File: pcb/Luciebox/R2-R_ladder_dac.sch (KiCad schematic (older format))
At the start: 12 parts, among them T2 terminal_8x1, T3 terminal_8x1, T4 terminal_8x1

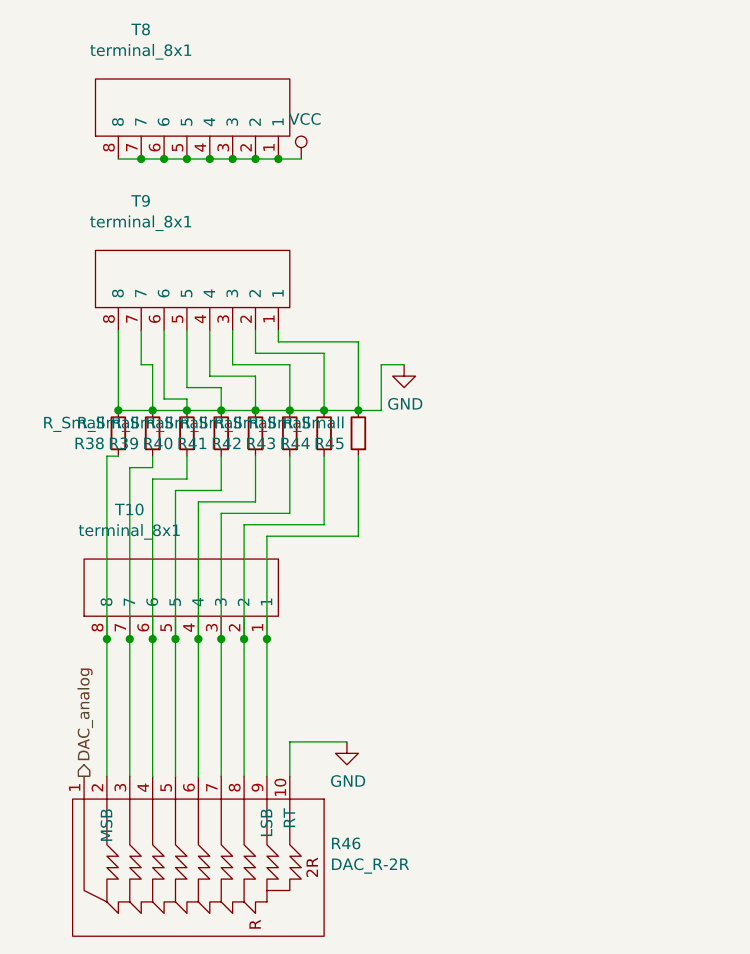
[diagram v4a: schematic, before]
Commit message: buttons and selector switch debugging. Starting to change pcb schematic for v2.0 board
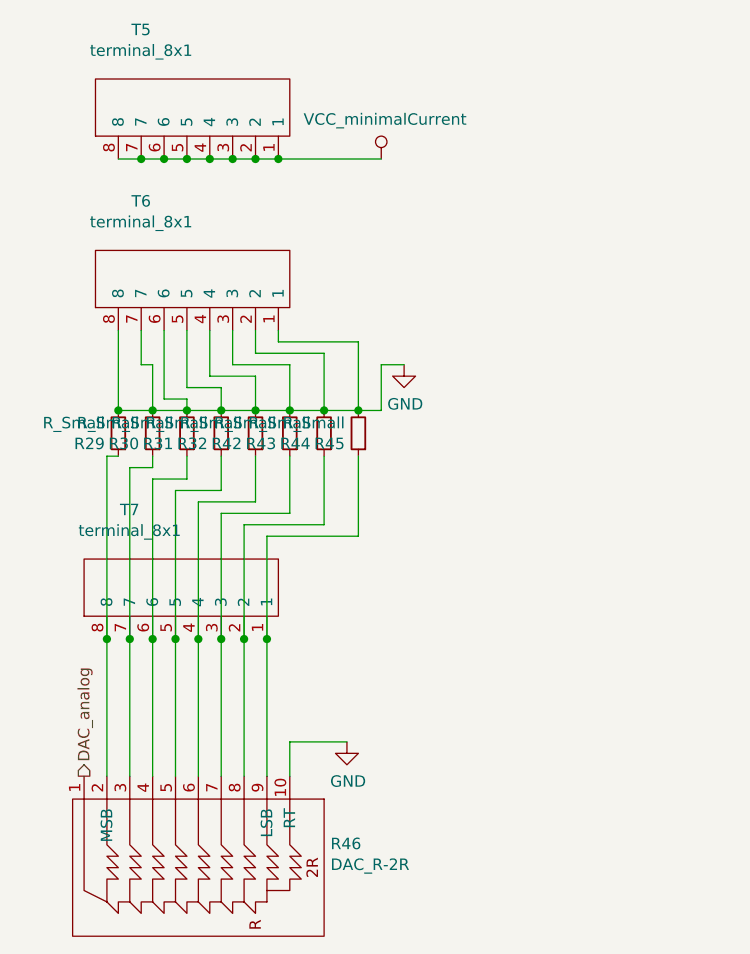
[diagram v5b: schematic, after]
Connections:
- net VCC renamed VCC_minimalCurrent
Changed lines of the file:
@@
 EESchema Schematic File Version 4
 LIBS:Luciebox-cache
-EELAYER 29 0
+EELAYER 30 0
 EELAYER END
 $Descr A4 11693 8268
@@
 AR Path="/5D761BCA/5D7526ED" Ref="R32"  Part="1"
 AR Path="/5D9307E8/5D7526ED" Ref="R41"  Part="1"
-F 0 "R41" H 3109 2246 50  0000 L CNN
+F 0 "R32" H 3109 2246 50  0000 L CNN
 F 1 "R_Small" H 3109 2155 50  0000 L CNN
 F 2 "Luciebox:1206" H 3050 2200 50  0001 C CNN
@@
 AR Path="/5D761BCA/5D7526F3" Ref="R31"  Part="1"
 AR Path="/5D9307E8/5D7526F3" Ref="R40"  Part="1"
-F 0 "R40" H 2959 2246 50  0000 L CNN
+F 0 "R31" H 2959 2246 50  0000 L CNN
 F 1 "R_Small" H 2959 2155 50  0000 L CNN
 F 2 "Luciebox:1206" H 2900 2200 50  0001 C CNN
@@
 AR Path="/5D761BCA/5D7526F9" Ref="R30"  Part="1"
 AR Path="/5D9307E8/5D7526F9" Ref="R39"  Part="1"
-F 0 "R39" H 2809 2246 50  0000 L CNN
+F 0 "R30" H 2809 2246 50  0000 L CNN
 F 1 "R_Small" H 2809 2155 50  0000 L CNN
 F 2 "Luciebox:1206" H 2750 2200 50  0001 C CNN
@@
 AR Path="/5D761BCA/5D75277B" Ref="#PWR023"  Part="1"
 AR Path="/5D9307E8/5D75277B" Ref="#PWR026"  Part="1"
-F 0 "#PWR026" H 3850 1650 50  0001 C CNN
+F 0 "#PWR023" H 3850 1650 50  0001 C CNN
 F 1 "GND" H 3855 1727 50  0000 C CNN
 F 2 "" H 3850 1900 50  0001 C CNN
@@
 AR Path="/5D761BCA/5D7527B8" Ref="R29"  Part="1"
 AR Path="/5D9307E8/5D7527B8" Ref="R38"  Part="1"
-F 0 "R38" H 2659 2246 50  0000 L CNN
+F 0 "R29" H 2659 2246 50  0000 L CNN
 F 1 "R_Small" H 2659 2155 50  0000 L CNN
 F 2 "Luciebox:1206" H 2600 2200 50  0001 C CNN
@@
 AR Path="/5D761BCA/5D7526D5" Ref="T7"  Part="1"
 AR Path="/5D9307E8/5D7526D5" Ref="T10"  Part="1"
-F 0 "T10" V 3765 3650 50  0000 C CNN
+F 0 "T7" V 3765 3650 50  0000 C CNN
 F 1 "terminal_8x1" V 3674 3650 50  0000 C CNN
 F 2 "Luciebox:Terminal_8x1_100mil" H 3250 3050 50  0001 C CNN
@@
 AR Path="/5D761BCA/5DACA23D" Ref="#PWR024"  Part="1"
 AR Path="/5D9307E8/5DACA23D" Ref="#PWR027"  Part="1"
-F 0 "#PWR027" H 3600 3300 50  0001 C CNN
+F 0 "#PWR024" H 3600 3300 50  0001 C CNN
 F 1 "GND" H 3605 3377 50  0000 C CNN
 F 2 "" H 3600 3550 50  0001 C CNN
@@
 AR Path="/5D761BCA/5DAEA72B" Ref="T6"  Part="1"
 AR Path="/5D9307E8/5DAEA72B" Ref="T9"  Part="1"
-F 0 "T9" V 3815 2300 50  0000 C CNN
+F 0 "T6" V 3815 2300 50  0000 C CNN
 F 1 "terminal_8x1" V 3724 2300 50  0000 C CNN
 F 2 "Luciebox:Terminal_8x1_100mil" H 3300 1700 50  0001 C CNN
@@
 AR Path="/5D761BCA/5DB0039D" Ref="T5"  Part="1"
 AR Path="/5D9307E8/5DB0039D" Ref="T8"  Part="1"
-F 0 "T8" V 3815 1550 50  0000 C CNN
+F 0 "T5" V 3815 1550 50  0000 C CNN
 F 1 "terminal_8x1" V 3724 1550 50  0000 C CNN
 F 2 "Luciebox:Terminal_8x1_100mil" H 3300 950 50  0001 C CNN
@@
 Wire Wire Line
 	3200 1000 3100 1000
-Wire Wire Line
-	3300 1000 3400 1000
 Connection ~ 3300 1000
 $Comp
-L power:VCC #PWR025
+L Luciebox_components:VCC_minimalCurrent #PWR025
 U 1 1 5DB05874
-P 3400 1000
+P 3750 1000
 AR Path="/5D9307E8/5DB05874" Ref="#PWR025"  Part="1"
 AR Path="/5D74964C/5DB05874" Ref="#PWR019"  Part="1"
 AR Path="/5D761BCA/5DB05874" Ref="#PWR022"  Part="1"
-F 0 "#PWR025" H 3400 850 50  0001 C CNN
-F 1 "VCC" H 3417 1173 50  0000 C CNN
-F 2 "" H 3400 1000 50  0001 C CNN
-F 3 "" H 3400 1000 50  0001 C CNN
-	1    3400 1000
+F 0 "#PWR022" H 3750 850 50  0001 C CNN
+F 1 "VCC_minimalCurrent" H 3767 1173 50  0000 C CNN
+F 2 "" H 3750 1000 50  0001 C CNN
+F 3 "" H 3750 1000 50  0001 C CNN
+	1    3750 1000
 	1    0    0    -1
 $EndComp
+Wire Wire Line
+	3300 1000 3750 1000
 $EndSCHEMATC

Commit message: changes in pcb v2.0
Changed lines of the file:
@@
 EESchema Schematic File Version 4
 LIBS:Luciebox-cache
-EELAYER 30 0
+EELAYER 29 0
 EELAYER END
 $Descr A4 11693 8268
 encoding utf-8
-Sheet 3 4
+Sheet 2 4
 Title ""
 Date ""
@@
 AR Path="/5D761BCA/5D7526CF" Ref="R36"  Part="1"
 AR Path="/5D9307E8/5D7526CF" Ref="R45"  Part="1"
-F 0 "R45" H 3709 2246 50  0000 L CNN
+F 0 "R36" H 3709 2246 50  0000 L CNN
 F 1 "R_Small" H 3709 2155 50  0000 L CNN
 F 2 "Luciebox:1206" H 3650 2200 50  0001 C CNN
@@
 $Comp
 L Device:R_Small R26
-U 1 1 5D7526DB
+U 1 1 5E6454DF
 P 3500 2200
-AR Path="/5D74964C/5D7526DB" Ref="R26"  Part="1"
-AR Path="/5D761BCA/5D7526DB" Ref="R35"  Part="1"
-AR Path="/5D9307E8/5D7526DB" Ref="R44"  Part="1"
-F 0 "R44" H 3559 2246 50  0000 L CNN
+AR Path="/5D74964C/5E6454DF" Ref="R26"  Part="1"
+AR Path="/5D761BCA/5E6454DF" Ref="R35"  Part="1"
+AR Path="/5D9307E8/5E6454DF" Ref="R44"  Part="1"
+F 0 "R35" H 3559 2246 50  0000 L CNN
 F 1 "R_Small" H 3559 2155 50  0000 L CNN
 F 2 "Luciebox:1206" H 3500 2200 50  0001 C CNN
@@
 $Comp
 L Device:R_Small R25
-U 1 1 5D7526E1
+U 1 1 5E6454E0
 P 3350 2200
-AR Path="/5D74964C/5D7526E1" Ref="R25"  Part="1"
-AR Path="/5D761BCA/5D7526E1" Ref="R34"  Part="1"
-AR Path="/5D9307E8/5D7526E1" Ref="R43"  Part="1"
-F 0 "R43" H 3409 2246 50  0000 L CNN
+AR Path="/5D74964C/5E6454E0" Ref="R25"  Part="1"
+AR Path="/5D761BCA/5E6454E0" Ref="R34"  Part="1"
+AR Path="/5D9307E8/5E6454E0" Ref="R43"  Part="1"
+F 0 "R34" H 3409 2246 50  0000 L CNN
 F 1 "R_Small" H 3409 2155 50  0000 L CNN
 F 2 "Luciebox:1206" H 3350 2200 50  0001 C CNN
@@
 $Comp
 L Device:R_Small R24
-U 1 1 5D7526E7
+U 1 1 5E6454E1
 P 3200 2200
-AR Path="/5D74964C/5D7526E7" Ref="R24"  Part="1"
-AR Path="/5D761BCA/5D7526E7" Ref="R33"  Part="1"
-AR Path="/5D9307E8/5D7526E7" Ref="R42"  Part="1"
-F 0 "R42" H 3259 2246 50  0000 L CNN
+AR Path="/5D74964C/5E6454E1" Ref="R24"  Part="1"
+AR Path="/5D761BCA/5E6454E1" Ref="R33"  Part="1"
+AR Path="/5D9307E8/5E6454E1" Ref="R42"  Part="1"
+F 0 "R33" H 3259 2246 50  0000 L CNN
 F 1 "R_Small" H 3259 2155 50  0000 L CNN
 F 2 "Luciebox:1206" H 3200 2200 50  0001 C CNN
@@
 $Comp
 L Luciebox_components:DAC_R-2R R28
-U 1 1 5DABC300
+U 1 1 5E6454E2
 P 2450 3700
-AR Path="/5D74964C/5DABC300" Ref="R28"  Part="1"
-AR Path="/5D761BCA/5DABC300" Ref="R37"  Part="1"
-AR Path="/5D9307E8/5DABC300" Ref="R46"  Part="1"
-F 0 "R46" V 2746 4778 50  0000 L CNN
+AR Path="/5D74964C/5E6454E2" Ref="R28"  Part="1"
+AR Path="/5D761BCA/5E6454E2" Ref="R37"  Part="1"
+AR Path="/5D9307E8/5E6454E2" Ref="R46"  Part="1"
+F 0 "R37" V 2746 4778 50  0000 L CNN
 F 1 "DAC_R-2R" V 2837 4778 50  0000 L CNN
 F 2 "Luciebox:SIP-10" H 2450 3700 50  0001 C CNN

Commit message: progressive change towards v2.0
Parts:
- R20, R21, R22, R23, R24, R25, R26, R27: footprint Luciebox:1206 -> Luciebox:1206_0805
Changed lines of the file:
@@
 $Descr A4 11693 8268
 encoding utf-8
-Sheet 2 4
+Sheet 3 4
 Title ""
 Date ""
@@
 F 0 "R36" H 3709 2246 50  0000 L CNN
 F 1 "R_Small" H 3709 2155 50  0000 L CNN
-F 2 "Luciebox:1206" H 3650 2200 50  0001 C CNN
+F 2 "Luciebox:1206_0805" H 3650 2200 50  0001 C CNN
 F 3 "~" H 3650 2200 50  0001 C CNN
 	1    3650 2200
@@
 F 0 "R35" H 3559 2246 50  0000 L CNN
 F 1 "R_Small" H 3559 2155 50  0000 L CNN
-F 2 "Luciebox:1206" H 3500 2200 50  0001 C CNN
+F 2 "Luciebox:1206_0805" H 3500 2200 50  0001 C CNN
 F 3 "~" H 3500 2200 50  0001 C CNN
 	1    3500 2200
@@
 F 0 "R34" H 3409 2246 50  0000 L CNN
 F 1 "R_Small" H 3409 2155 50  0000 L CNN
-F 2 "Luciebox:1206" H 3350 2200 50  0001 C CNN
+F 2 "Luciebox:1206_0805" H 3350 2200 50  0001 C CNN
 F 3 "~" H 3350 2200 50  0001 C CNN
 	1    3350 2200
@@
 F 0 "R33" H 3259 2246 50  0000 L CNN
 F 1 "R_Small" H 3259 2155 50  0000 L CNN
-F 2 "Luciebox:1206" H 3200 2200 50  0001 C CNN
+F 2 "Luciebox:1206_0805" H 3200 2200 50  0001 C CNN
 F 3 "~" H 3200 2200 50  0001 C CNN
 	1    3200 2200
@@
 F 0 "R32" H 3109 2246 50  0000 L CNN
 F 1 "R_Small" H 3109 2155 50  0000 L CNN
-F 2 "Luciebox:1206" H 3050 2200 50  0001 C CNN
+F 2 "Luciebox:1206_0805" H 3050 2200 50  0001 C CNN
 F 3 "~" H 3050 2200 50  0001 C CNN
 	1    3050 2200
@@
 F 0 "R31" H 2959 2246 50  0000 L CNN
 F 1 "R_Small" H 2959 2155 50  0000 L CNN
-F 2 "Luciebox:1206" H 2900 2200 50  0001 C CNN
+F 2 "Luciebox:1206_0805" H 2900 2200 50  0001 C CNN
 F 3 "~" H 2900 2200 50  0001 C CNN
 	1    2900 2200
@@
 F 0 "R30" H 2809 2246 50  0000 L CNN
 F 1 "R_Small" H 2809 2155 50  0000 L CNN
-F 2 "Luciebox:1206" H 2750 2200 50  0001 C CNN
+F 2 "Luciebox:1206_0805" H 2750 2200 50  0001 C CNN
 F 3 "~" H 2750 2200 50  0001 C CNN
 	1    2750 2200
@@
 F 0 "R29" H 2659 2246 50  0000 L CNN
 F 1 "R_Small" H 2659 2155 50  0000 L CNN
-F 2 "Luciebox:1206" H 2600 2200 50  0001 C CNN
+F 2 "Luciebox:1206_0805" H 2600 2200 50  0001 C CNN
 F 3 "~" H 2600 2200 50  0001 C CNN
 	1    2600 2200

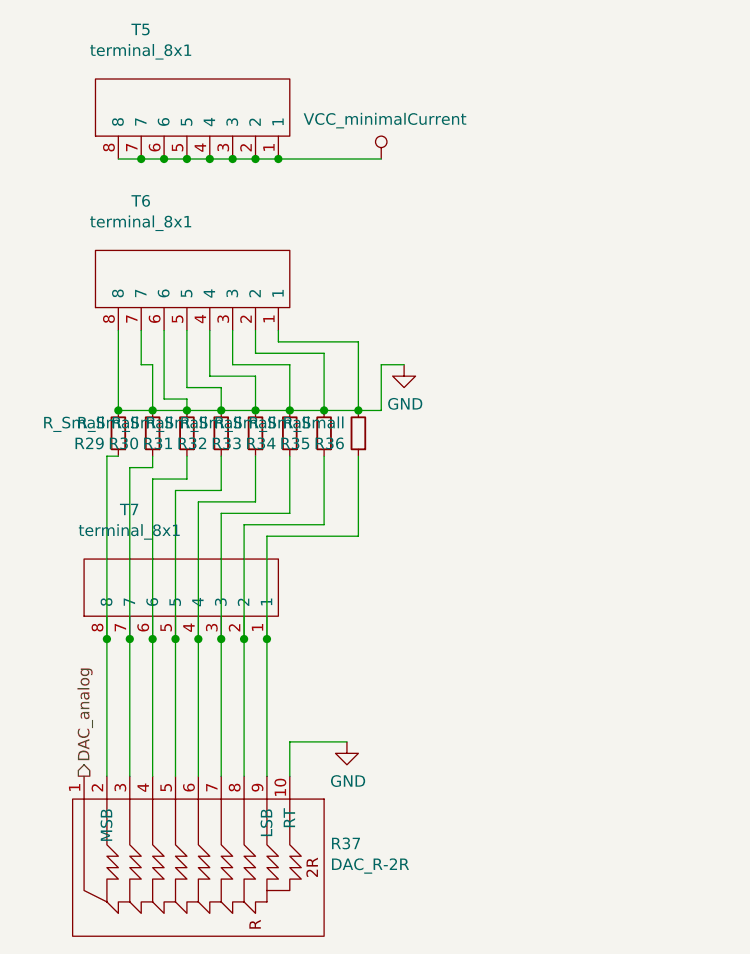
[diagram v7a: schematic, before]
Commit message: add holes for R-2R ladder, fix bug with tilt switch sheet. Set output led's. All good here.
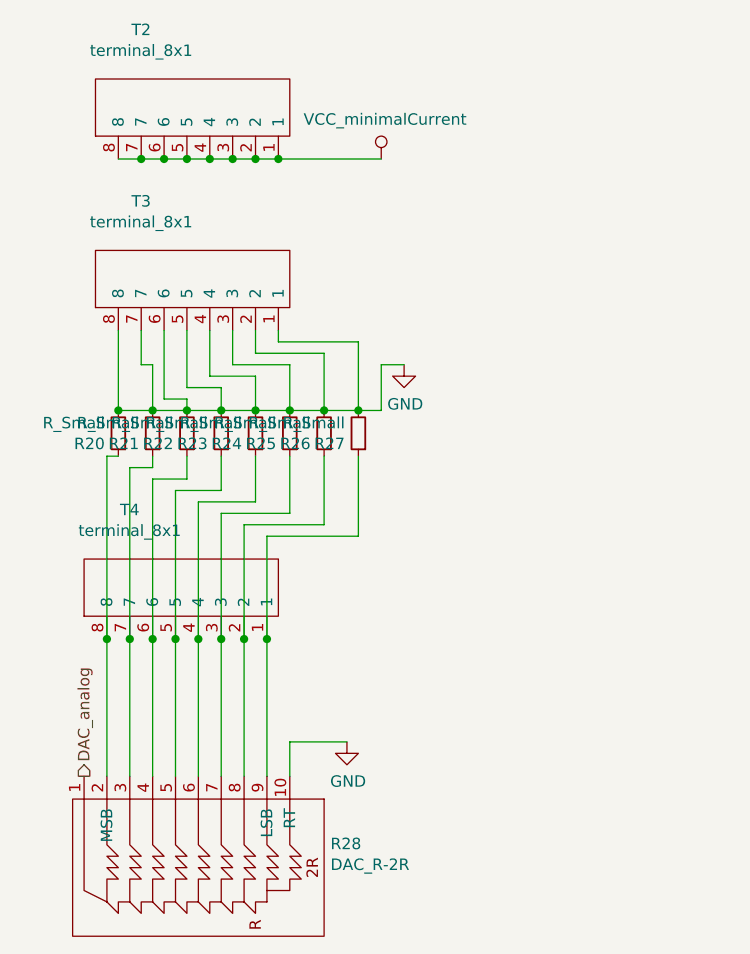
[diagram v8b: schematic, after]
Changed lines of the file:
@@
 $Descr A4 11693 8268
 encoding utf-8
-Sheet 3 4
+Sheet 2 4
 Title ""
 Date ""
@@
 AR Path="/5D761BCA/5D7526CF" Ref="R36"  Part="1"
 AR Path="/5D9307E8/5D7526CF" Ref="R45"  Part="1"
-F 0 "R36" H 3709 2246 50  0000 L CNN
+F 0 "R27" H 3709 2246 50  0000 L CNN
 F 1 "R_Small" H 3709 2155 50  0000 L CNN
 F 2 "Luciebox:1206_0805" H 3650 2200 50  0001 C CNN
@@
 AR Path="/5D761BCA/5E6454DF" Ref="R35"  Part="1"
 AR Path="/5D9307E8/5E6454DF" Ref="R44"  Part="1"
-F 0 "R35" H 3559 2246 50  0000 L CNN
+F 0 "R26" H 3559 2246 50  0000 L CNN
 F 1 "R_Small" H 3559 2155 50  0000 L CNN
 F 2 "Luciebox:1206_0805" H 3500 2200 50  0001 C CNN
@@
 AR Path="/5D761BCA/5E6454E0" Ref="R34"  Part="1"
 AR Path="/5D9307E8/5E6454E0" Ref="R43"  Part="1"
-F 0 "R34" H 3409 2246 50  0000 L CNN
+F 0 "R25" H 3409 2246 50  0000 L CNN
 F 1 "R_Small" H 3409 2155 50  0000 L CNN
 F 2 "Luciebox:1206_0805" H 3350 2200 50  0001 C CNN
@@
 AR Path="/5D761BCA/5E6454E1" Ref="R33"  Part="1"
 AR Path="/5D9307E8/5E6454E1" Ref="R42"  Part="1"
-F 0 "R33" H 3259 2246 50  0000 L CNN
+F 0 "R24" H 3259 2246 50  0000 L CNN
 F 1 "R_Small" H 3259 2155 50  0000 L CNN
 F 2 "Luciebox:1206_0805" H 3200 2200 50  0001 C CNN
@@
 AR Path="/5D761BCA/5D7526ED" Ref="R32"  Part="1"
 AR Path="/5D9307E8/5D7526ED" Ref="R41"  Part="1"
-F 0 "R32" H 3109 2246 50  0000 L CNN
+F 0 "R23" H 3109 2246 50  0000 L CNN
 F 1 "R_Small" H 3109 2155 50  0000 L CNN
 F 2 "Luciebox:1206_0805" H 3050 2200 50  0001 C CNN
@@
 AR Path="/5D761BCA/5D7526F3" Ref="R31"  Part="1"
 AR Path="/5D9307E8/5D7526F3" Ref="R40"  Part="1"
-F 0 "R31" H 2959 2246 50  0000 L CNN
+F 0 "R22" H 2959 2246 50  0000 L CNN
 F 1 "R_Small" H 2959 2155 50  0000 L CNN
 F 2 "Luciebox:1206_0805" H 2900 2200 50  0001 C CNN
@@
 AR Path="/5D761BCA/5D7526F9" Ref="R30"  Part="1"
 AR Path="/5D9307E8/5D7526F9" Ref="R39"  Part="1"
-F 0 "R30" H 2809 2246 50  0000 L CNN
+F 0 "R21" H 2809 2246 50  0000 L CNN
 F 1 "R_Small" H 2809 2155 50  0000 L CNN
 F 2 "Luciebox:1206_0805" H 2750 2200 50  0001 C CNN
@@
 AR Path="/5D761BCA/5D7527B8" Ref="R29"  Part="1"
 AR Path="/5D9307E8/5D7527B8" Ref="R38"  Part="1"
-F 0 "R29" H 2659 2246 50  0000 L CNN
+F 0 "R20" H 2659 2246 50  0000 L CNN
 F 1 "R_Small" H 2659 2155 50  0000 L CNN
 F 2 "Luciebox:1206_0805" H 2600 2200 50  0001 C CNN
@@
 AR Path="/5D761BCA/5E6454E2" Ref="R37"  Part="1"
 AR Path="/5D9307E8/5E6454E2" Ref="R46"  Part="1"
-F 0 "R37" V 2746 4778 50  0000 L CNN
+F 0 "R28" V 2746 4778 50  0000 L CNN
 F 1 "DAC_R-2R" V 2837 4778 50  0000 L CNN
 F 2 "Luciebox:SIP-10" H 2450 3700 50  0001 C CNN
@@
 AR Path="/5D761BCA/5D7526D5" Ref="T7"  Part="1"
 AR Path="/5D9307E8/5D7526D5" Ref="T10"  Part="1"
-F 0 "T7" V 3765 3650 50  0000 C CNN
+F 0 "T4" V 3765 3650 50  0000 C CNN
 F 1 "terminal_8x1" V 3674 3650 50  0000 C CNN
 F 2 "Luciebox:Terminal_8x1_100mil" H 3250 3050 50  0001 C CNN
@@
 AR Path="/5D761BCA/5DAEA72B" Ref="T6"  Part="1"
 AR Path="/5D9307E8/5DAEA72B" Ref="T9"  Part="1"
-F 0 "T6" V 3815 2300 50  0000 C CNN
+F 0 "T3" V 3815 2300 50  0000 C CNN
 F 1 "terminal_8x1" V 3724 2300 50  0000 C CNN
 F 2 "Luciebox:Terminal_8x1_100mil" H 3300 1700 50  0001 C CNN
@@
 AR Path="/5D761BCA/5DB0039D" Ref="T5"  Part="1"
 AR Path="/5D9307E8/5DB0039D" Ref="T8"  Part="1"
-F 0 "T5" V 3815 1550 50  0000 C CNN
+F 0 "T2" V 3815 1550 50  0000 C CNN
 F 1 "terminal_8x1" V 3724 1550 50  0000 C CNN
 F 2 "Luciebox:Terminal_8x1_100mil" H 3300 950 50  0001 C CNN
